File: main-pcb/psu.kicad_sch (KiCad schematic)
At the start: 124 parts, among them J1 CONN_01X03, J2 CORTEX_DEBUG_ETM, SW1 SWITCH, SW2 SWITCH, U10 NCP45525IMNTWG-H, U11 LTC3374-QFN, U19 INA230, U2 STM32L431-QFN48, U3 INA230, U4 INA230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

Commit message: Under 400 unrouted
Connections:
- net DUT_VCCIO_EN: now also U2.33 (PA12); no longer U2.45 (PB8)
- net SUPER_FAULT_LED: now also U2.45 (PB8); no longer U2.33 (PA12)
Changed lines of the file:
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@@
 	)
 	(label "SUPER_FAULT_LED"
-		(at 255.27 93.98 180)
+		(at 255.27 163.83 180)
 		(fields_autoplaced yes)
 		(effects
@@
 	(hierarchical_label "DUT_VCCIO_EN"
 		(shape output)
-		(at 255.27 163.83 180)
-		(fields_autoplaced yes)
-		(effects
+		(at 255.27 93.98 180)
+		(fields_autoplaced yes)
+		(effects

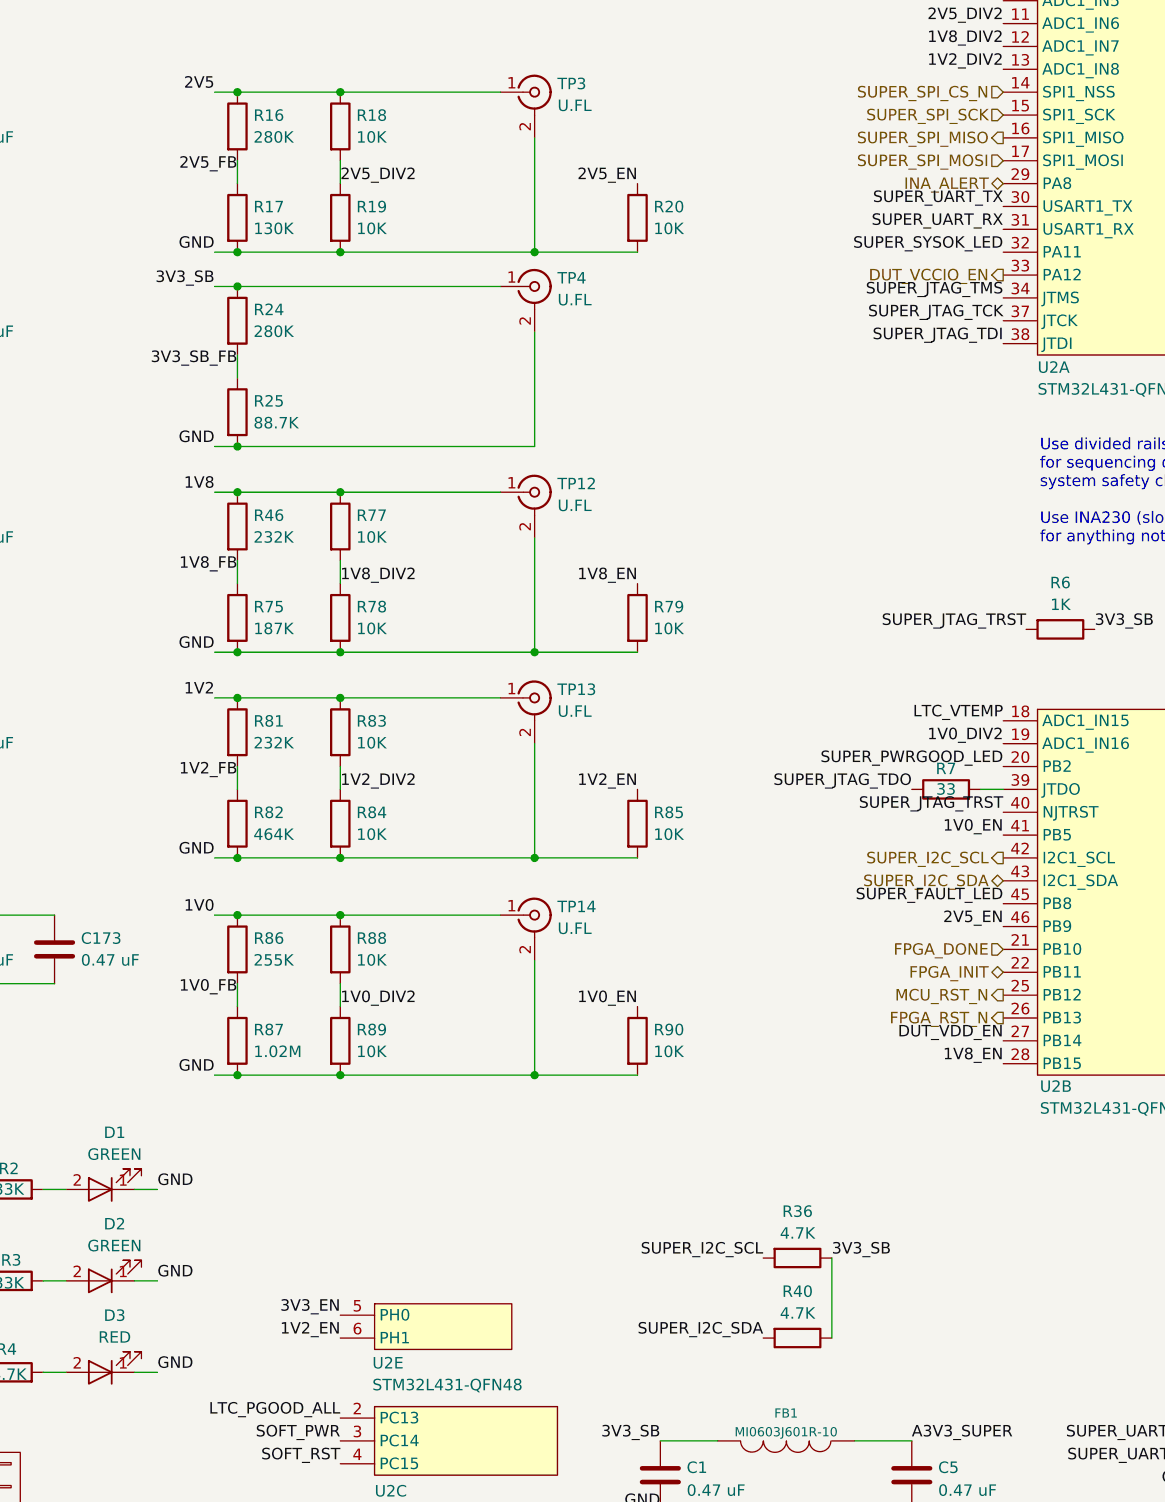
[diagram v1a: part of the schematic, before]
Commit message: Continued routing RGMII PHY
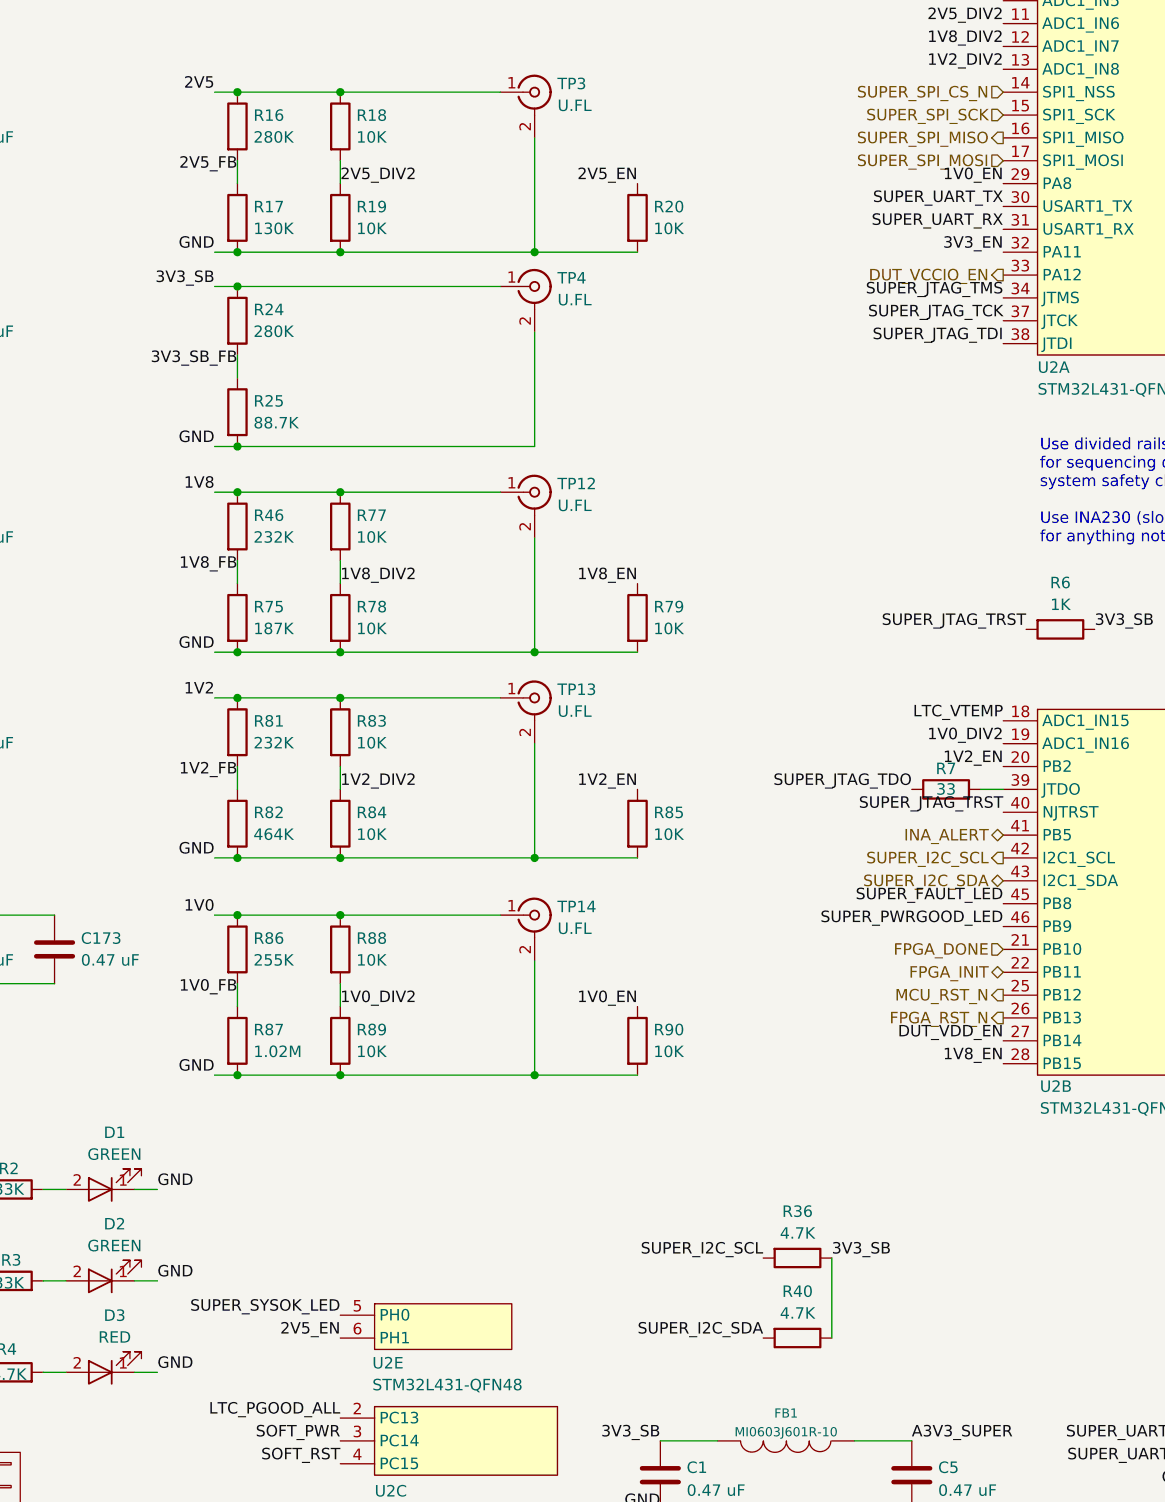
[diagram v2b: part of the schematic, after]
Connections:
- net 1V0_EN: now also U2.29 (PA8); no longer U2.41 (PB5)
- net 1V2_EN: now also U2.20 (PB2); no longer U2.6 (PH1)
- net 2V5_EN: now also U2.6 (PH1); no longer U2.46 (PB9)
- net 3V3_EN: now also U2.32 (PA11); no longer U2.5 (PH0)
- net INA_ALERT: now also U2.41 (PB5); no longer U2.29 (PA8)
- net SUPER_PWRGOOD_LED: now also U2.46 (PB9); no longer U2.20 (PB2)
- net SUPER_SYSOK_LED: now also U2.5 (PH0); no longer U2.32 (PA11)
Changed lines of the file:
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@@
 	)
 	(label "2V5_EN"
-		(at 255.27 166.37 180)
+		(at 181.61 212.09 180)
 		(fields_autoplaced yes)
 		(effects
@@
 	)
 	(label "1V2_EN"
-		(at 181.61 212.09 180)
+		(at 255.27 148.59 180)
 		(fields_autoplaced yes)
 		(effects
@@
 	)
 	(label "SUPER_PWRGOOD_LED"
-		(at 255.27 148.59 180)
+		(at 255.27 166.37 180)
 		(fields_autoplaced yes)
 		(effects
@@
 	)
 	(label "1V0_EN"
-		(at 255.27 156.21 180)
+		(at 255.27 83.82 180)
 		(fields_autoplaced yes)
 		(effects
@@
 	)
 	(label "3V3_EN"
-		(at 181.61 209.55 180)
+		(at 255.27 91.44 180)
 		(fields_autoplaced yes)
 		(effects
@@
 	)
 	(label "SUPER_SYSOK_LED"
-		(at 255.27 91.44 180)
+		(at 181.61 209.55 180)
 		(fields_autoplaced yes)
 		(effects
@@
 	(hierarchical_label "INA_ALERT"
 		(shape bidirectional)
-		(at 255.27 83.82 180)
-		(fields_autoplaced yes)
-		(effects
+		(at 255.27 156.21 180)
+		(fields_autoplaced yes)
+		(effects

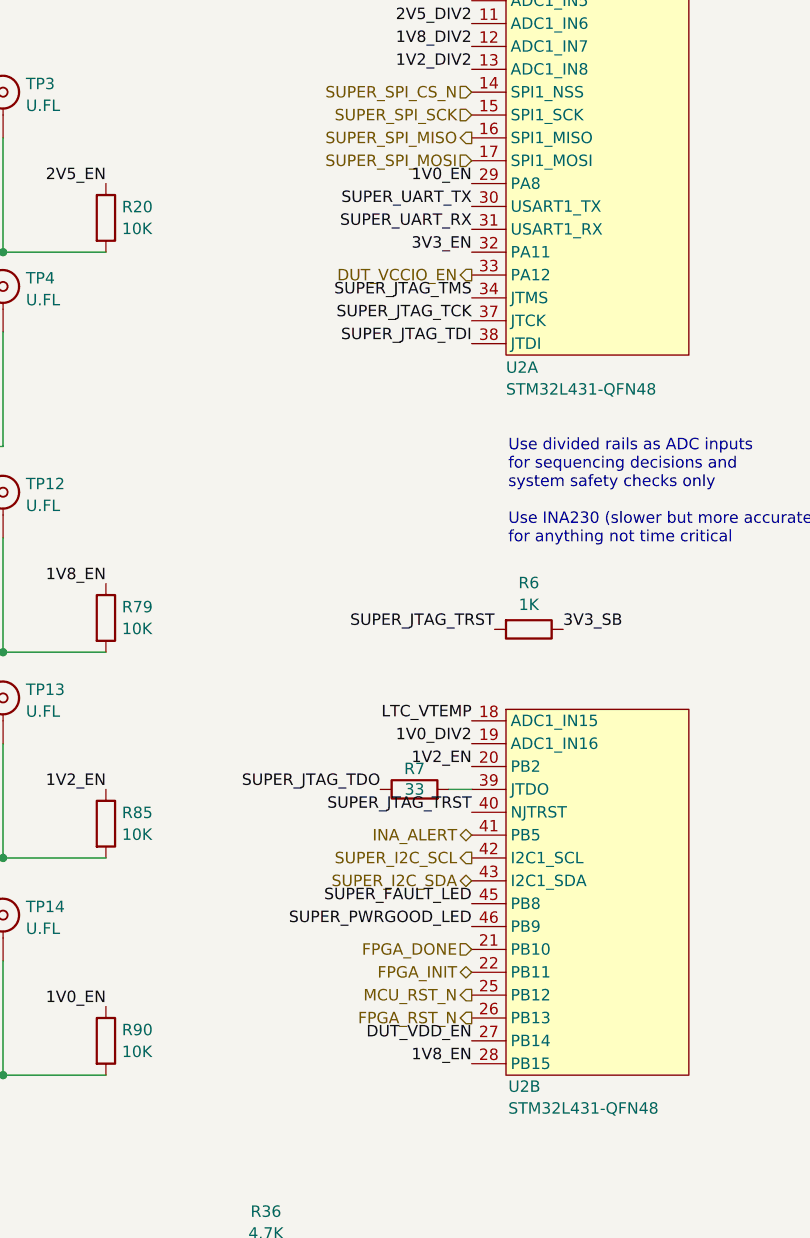
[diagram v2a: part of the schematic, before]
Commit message: Almost fully routed MCU
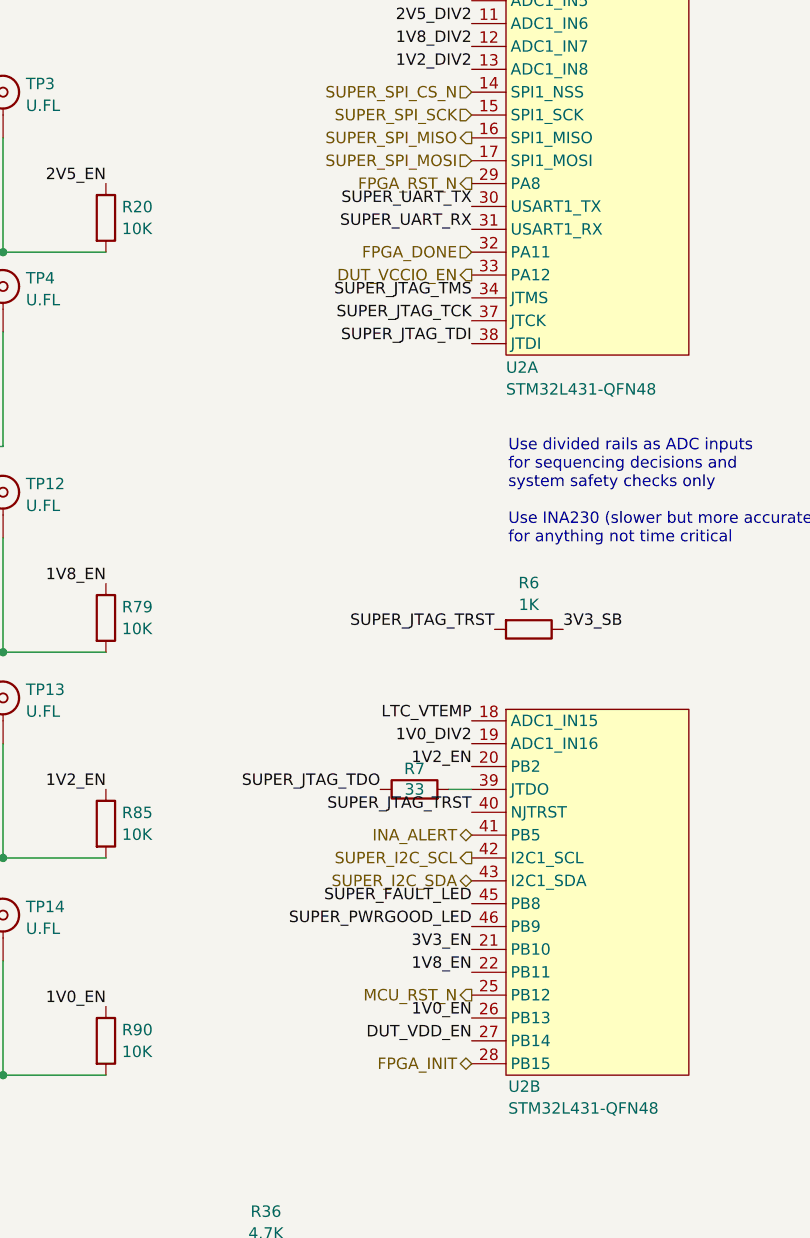
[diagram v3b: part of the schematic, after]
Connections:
- net 1V0_EN: now also U2.26 (PB13); no longer U2.29 (PA8)
- net 1V8_EN: now also U2.22 (PB11); no longer U2.28 (PB15)
- net 3V3_EN: now also U2.21 (PB10); no longer U2.32 (PA11)
- net FPGA_DONE: now also U2.32 (PA11); no longer U2.21 (PB10)
- net FPGA_INIT: now also U2.28 (PB15); no longer U2.22 (PB11)
- net FPGA_RST_N: now also U2.29 (PA8); no longer U2.26 (PB13)
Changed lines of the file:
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@@
 	)
 	(label "1V0_EN"
-		(at 255.27 83.82 180)
+		(at 255.27 176.53 180)
 		(fields_autoplaced yes)
 		(effects
@@
 	)
 	(label "3V3_EN"
-		(at 255.27 91.44 180)
+		(at 255.27 168.91 180)
 		(fields_autoplaced yes)
 		(effects
@@
 	)
 	(label "1V8_EN"
-		(at 255.27 181.61 180)
+		(at 255.27 171.45 180)
 		(fields_autoplaced yes)
 		(effects
@@
 	(hierarchical_label "FPGA_INIT"
 		(shape bidirectional)
-		(at 255.27 171.45 180)
+		(at 255.27 181.61 180)
 		(fields_autoplaced yes)
 		(effects
@@
 	(hierarchical_label "FPGA_RST_N"
 		(shape output)
-		(at 255.27 176.53 180)
+		(at 255.27 83.82 180)
 		(fields_autoplaced yes)
 		(effects
@@
 	(hierarchical_label "FPGA_DONE"
 		(shape input)
-		(at 255.27 168.91 180)
-		(fields_autoplaced yes)
-		(effects
+		(at 255.27 91.44 180)
+		(fields_autoplaced yes)
+		(effects

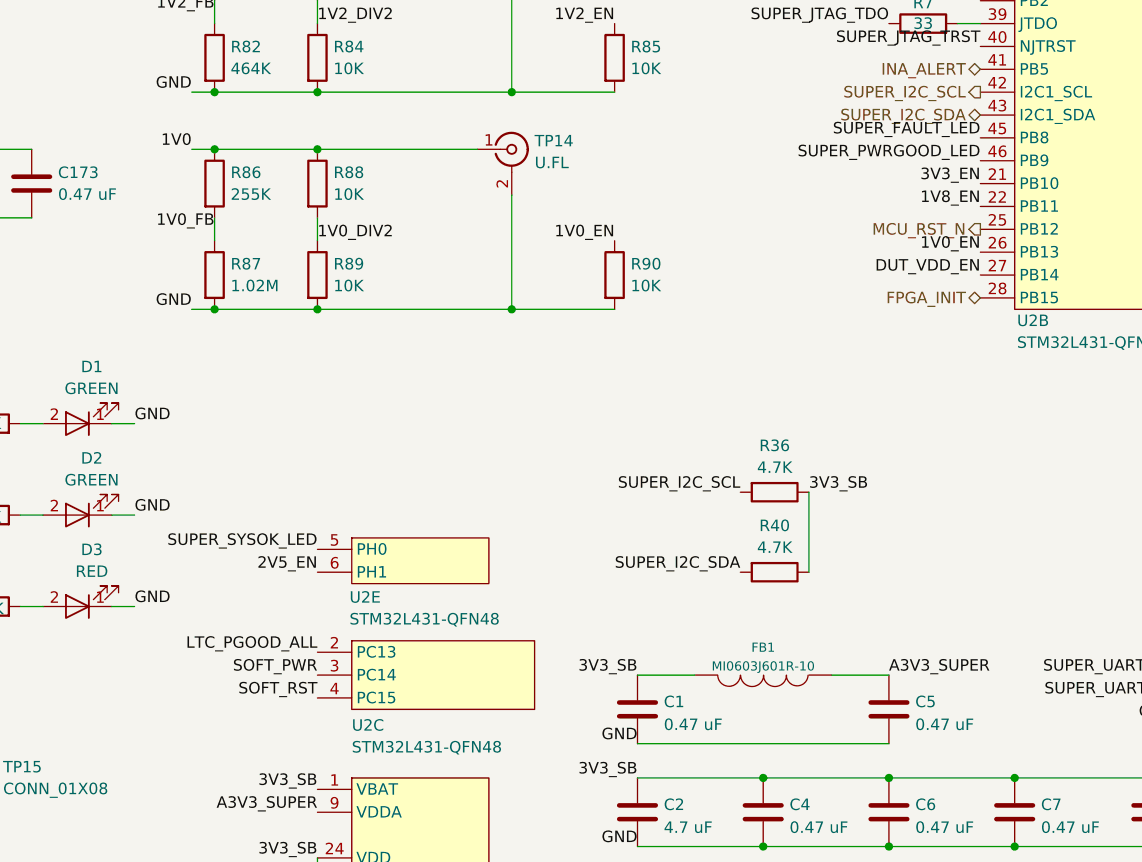
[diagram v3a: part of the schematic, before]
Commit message: Continued routing power supply
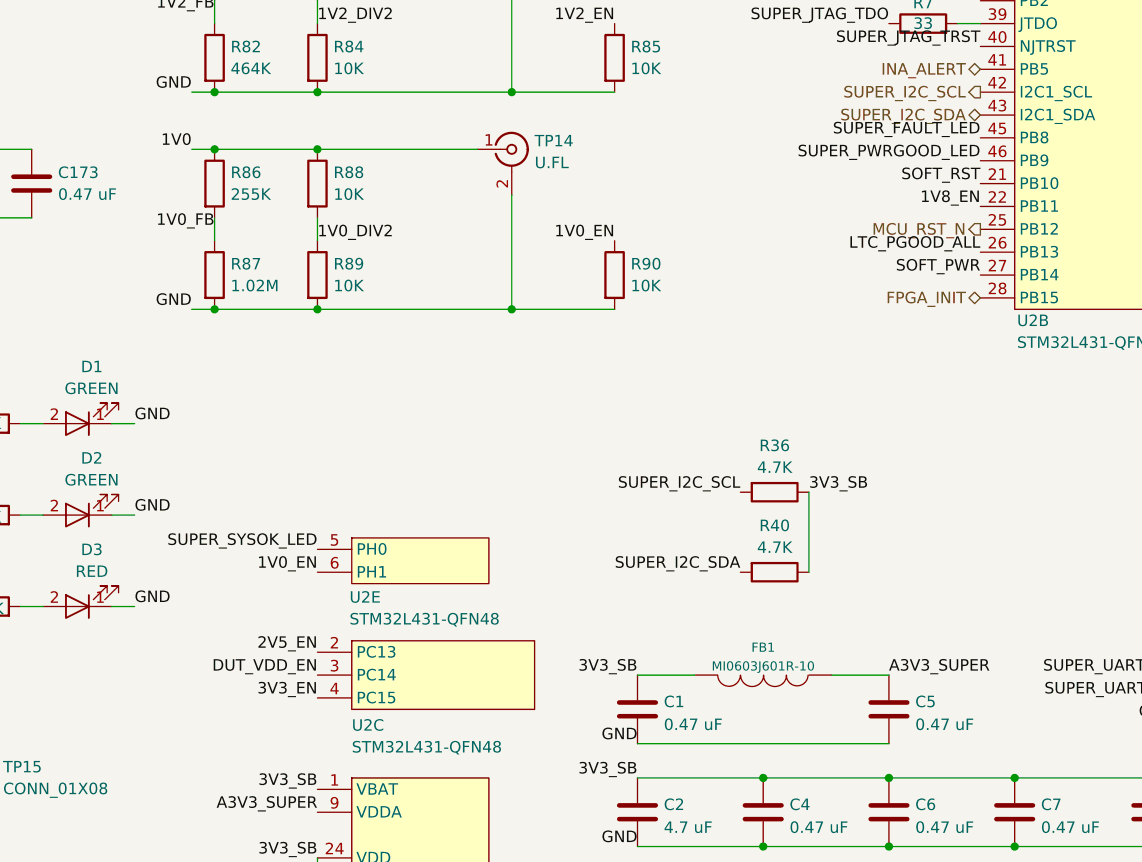
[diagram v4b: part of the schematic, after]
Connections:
- net 1V0_EN: now also U2.6 (PH1); no longer U2.26 (PB13)
- net 2V5_EN: now also U2.2 (PC13); no longer U2.6 (PH1)
- net 3V3_EN: now also U2.4 (PC15); no longer U2.21 (PB10)
- net DUT_VDD_EN: now also U2.3 (PC14); no longer U2.27 (PB14)
- net LTC_PGOOD_ALL: now also U2.26 (PB13); no longer U2.2 (PC13)
- net SOFT_PWR: now also U2.27 (PB14); no longer U2.3 (PC14)
- net SOFT_RST: now also U2.21 (PB10); no longer U2.4 (PC15)
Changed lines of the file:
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@@
 	)
 	(label "2V5_EN"
-		(at 181.61 212.09 180)
+		(at 181.61 220.98 180)
 		(fields_autoplaced yes)
 		(effects
@@
 	)
 	(label "SOFT_RST"
-		(at 181.61 226.06 180)
+		(at 255.27 168.91 180)
 		(fields_autoplaced yes)
 		(effects
@@
 	)
 	(label "DUT_VDD_EN"
-		(at 255.27 179.07 180)
+		(at 181.61 223.52 180)
 		(fields_autoplaced yes)
 		(effects
@@
 	)
 	(label "1V0_EN"
-		(at 255.27 176.53 180)
+		(at 181.61 212.09 180)
 		(fields_autoplaced yes)
 		(effects
@@
 	)
 	(label "3V3_EN"
-		(at 255.27 168.91 180)
+		(at 181.61 226.06 180)
 		(fields_autoplaced yes)
 		(effects
@@
 	)
 	(label "LTC_PGOOD_ALL"
-		(at 181.61 220.98 180)
+		(at 255.27 176.53 180)
 		(fields_autoplaced yes)
 		(effects
@@
 	)
 	(label "SOFT_PWR"
-		(at 181.61 223.52 180)
-		(fields_autoplaced yes)
-		(effects
+		(at 255.27 179.07 180)
+		(fields_autoplaced yes)
+		(effects
